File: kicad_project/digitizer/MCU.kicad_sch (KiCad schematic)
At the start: 4 parts

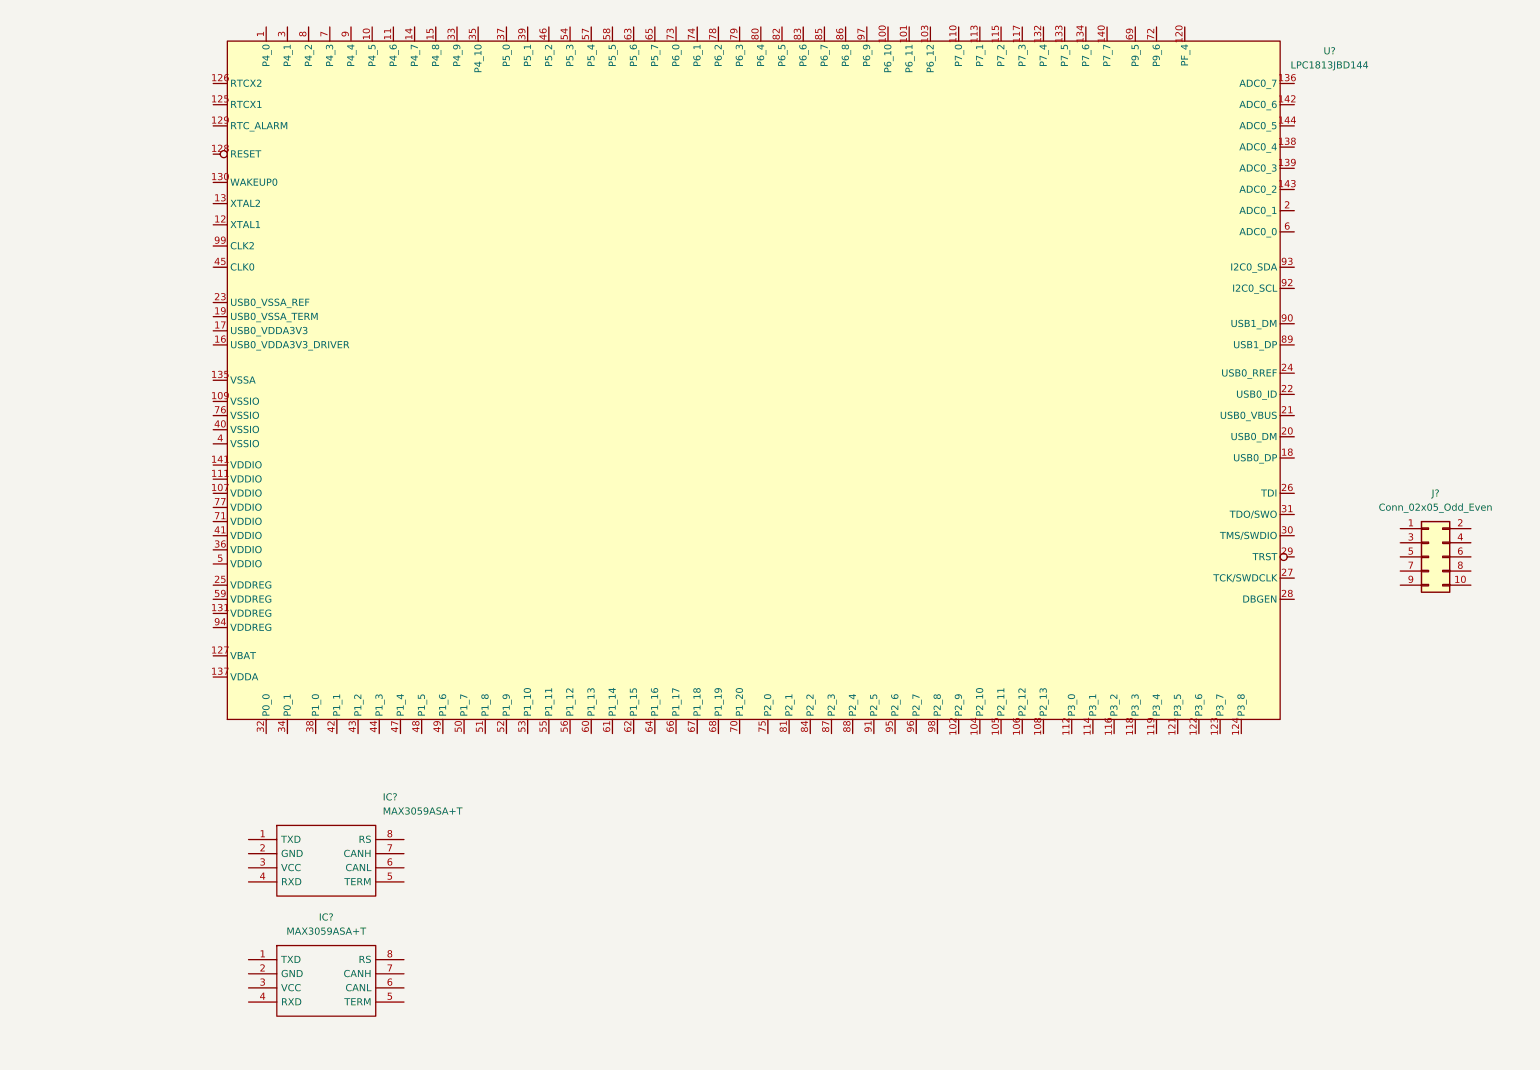
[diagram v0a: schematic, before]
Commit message: finished the CANPWR sheet, got to work on the MCU sheet (finished the CAN stuff). Good progress; still missing the MCU pin connections and the connector footprints (M12, deutsch, etc.)
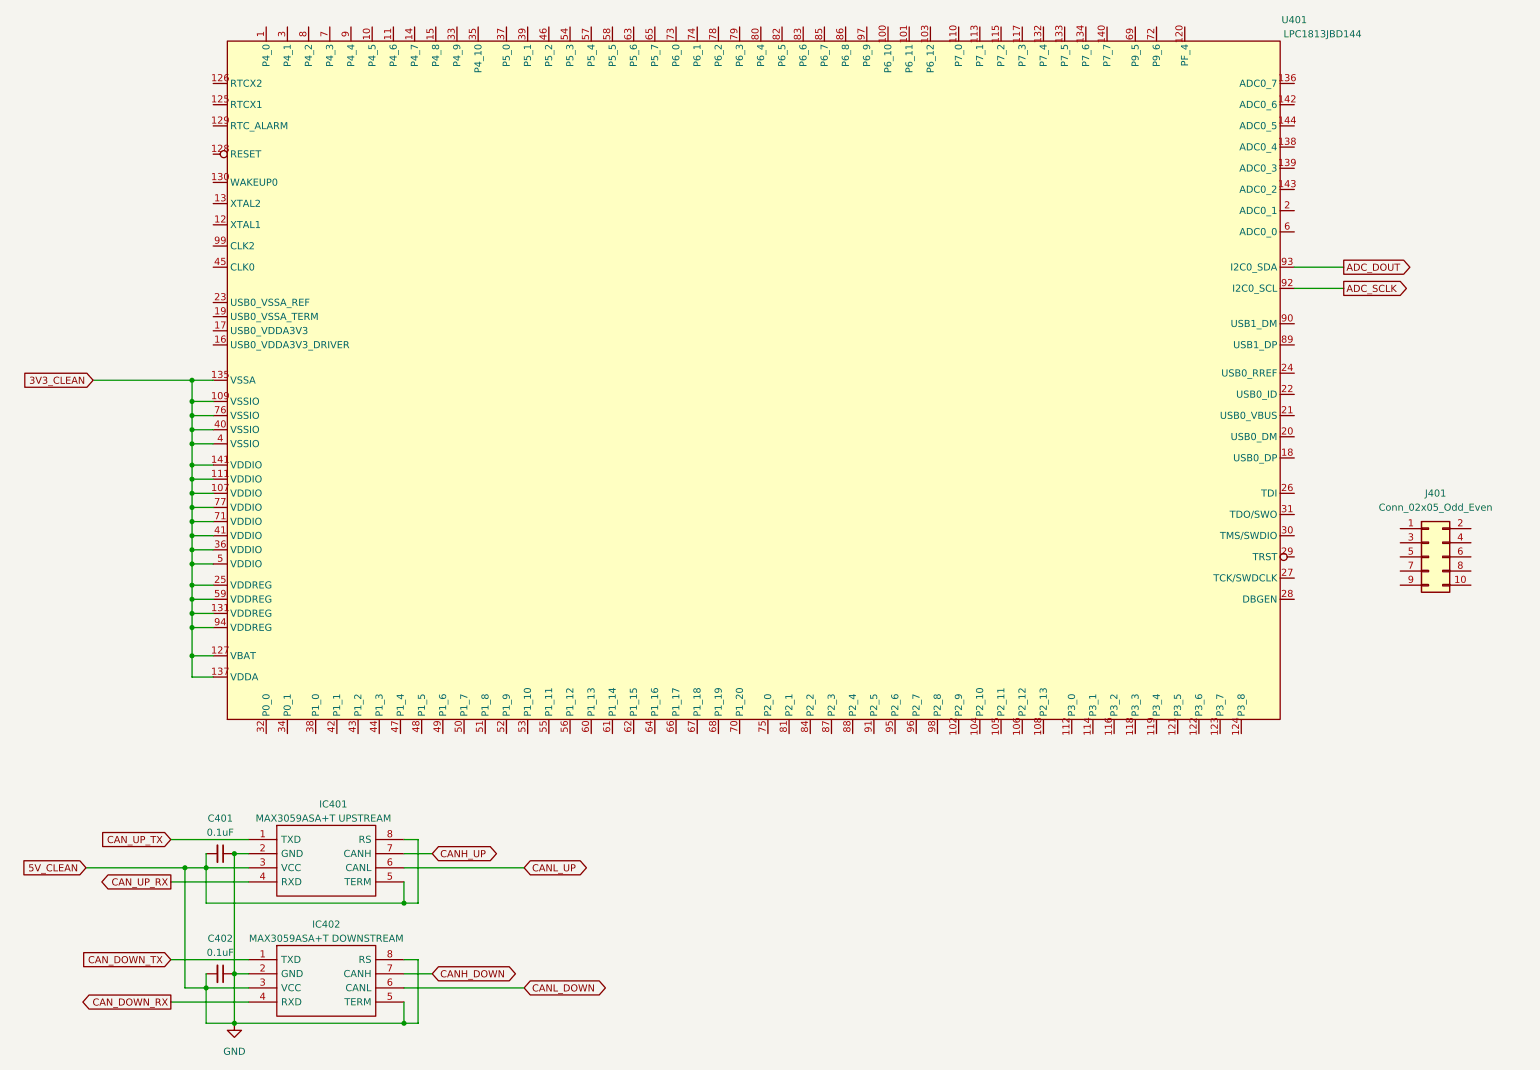
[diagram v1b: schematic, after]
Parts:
- added C401, C402: 0.1uF, Capacitor_SMD:C_2220_5650Metric_Pad1.97x5.40mm_HandSolder, symbol Device:C_Small
- IC401: renamed from IC?; value MAX3059ASA+T -> MAX3059ASA+T UPSTREAM
- IC402: renamed from IC?; value MAX3059ASA+T -> MAX3059ASA+T DOWNSTREAM
- gave numbers to parts that had none: 2
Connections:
- net CAN_DOWN_TX: now reaches IC402.1 (TXD)
- net GND: now reaches IC402.2 (GND)
- net GND: now also IC401.2 (GND), IC401.3 (VCC), IC401.5 (TERM), IC401.8 (RS), IC402.3 (VCC), IC402.5 (TERM), IC402.8 (RS), C401.1, C401.2, C402.1, C402.2
- net CAN_DOWN_RX: now reaches IC402.4 (RXD)
- net CANL_DOWN: now reaches IC402.6 (CANL)
- net CANH_DOWN: now reaches IC402.7 (CANH)
- net 3V3_CLEAN: now reaches U401.107 (VDDIO)
- net 3V3_CLEAN: now also U401.109 (VSSIO), U401.111 (VDDIO), U401.127 (VBAT), U401.131 (VDDREG), U401.135 (VSSA), U401.137 (VDDA), U401.141 (VDDIO), U401.25 (VDDREG), U401.36 (VDDIO), U401.4 (VSSIO), U401.40 (VSSIO), U401.41 (VDDIO), U401.5 (VDDIO), U401.59 (VDDREG), U401.71 (VDDIO), U401.76 (VSSIO), U401.77 (VDDIO), U401.94 (VDDREG)
- net ADC_SCLK: now reaches U401.92 (I2C0_SCL)
- net ADC_DOUT: now reaches U401.93 (I2C0_SDA)
- net CAN_UP_TX: now reaches IC401.1 (TXD)
- net CAN_UP_RX: now reaches IC401.4 (RXD)
- net CANL_UP: now reaches IC401.6 (CANL)
- net CANH_UP: now reaches IC401.7 (CANH)

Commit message: commit
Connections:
- net 3V3_CLEAN: no longer U401.109 (VSSIO), U401.135 (VSSA), U401.4 (VSSIO), U401.40 (VSSIO), U401.76 (VSSIO)
- net GND: now also U401.109 (VSSIO), U401.135 (VSSA), U401.4 (VSSIO), U401.40 (VSSIO), U401.76 (VSSIO)

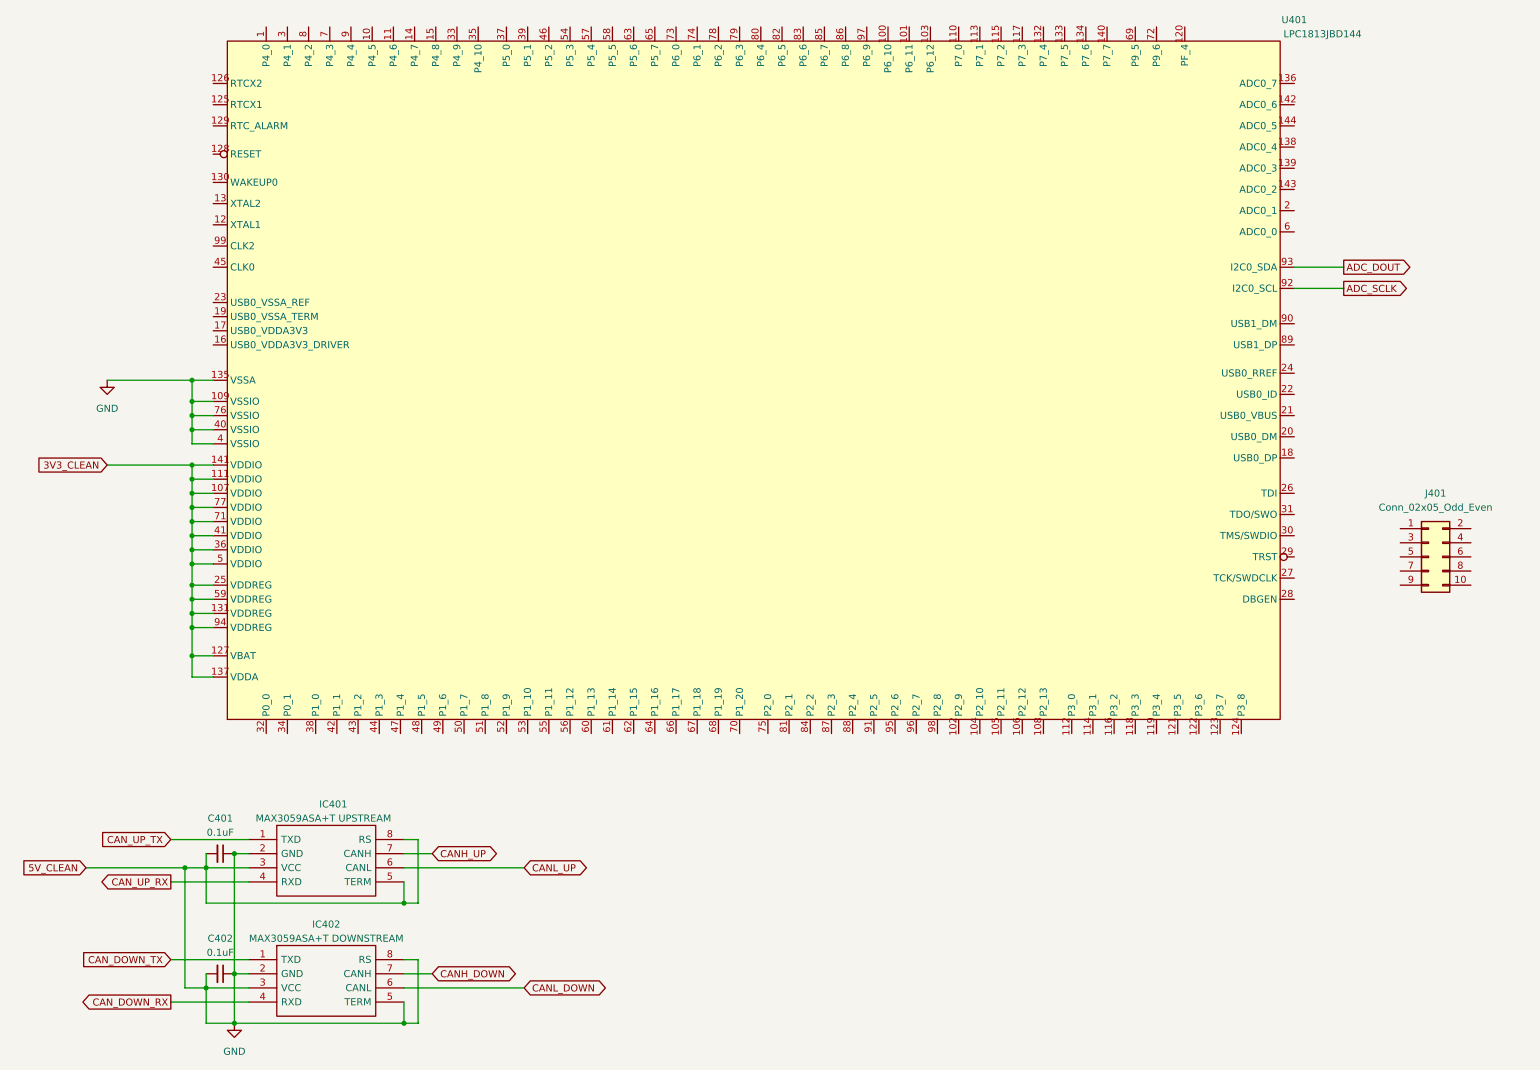
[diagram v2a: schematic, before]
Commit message: imported the correct symbols & footprints, and added a few to the schematic: pulled in the correct MCU symbol/footprint, as well as the correct JTAG footprint (connected to the 2x5 odd_even connector)
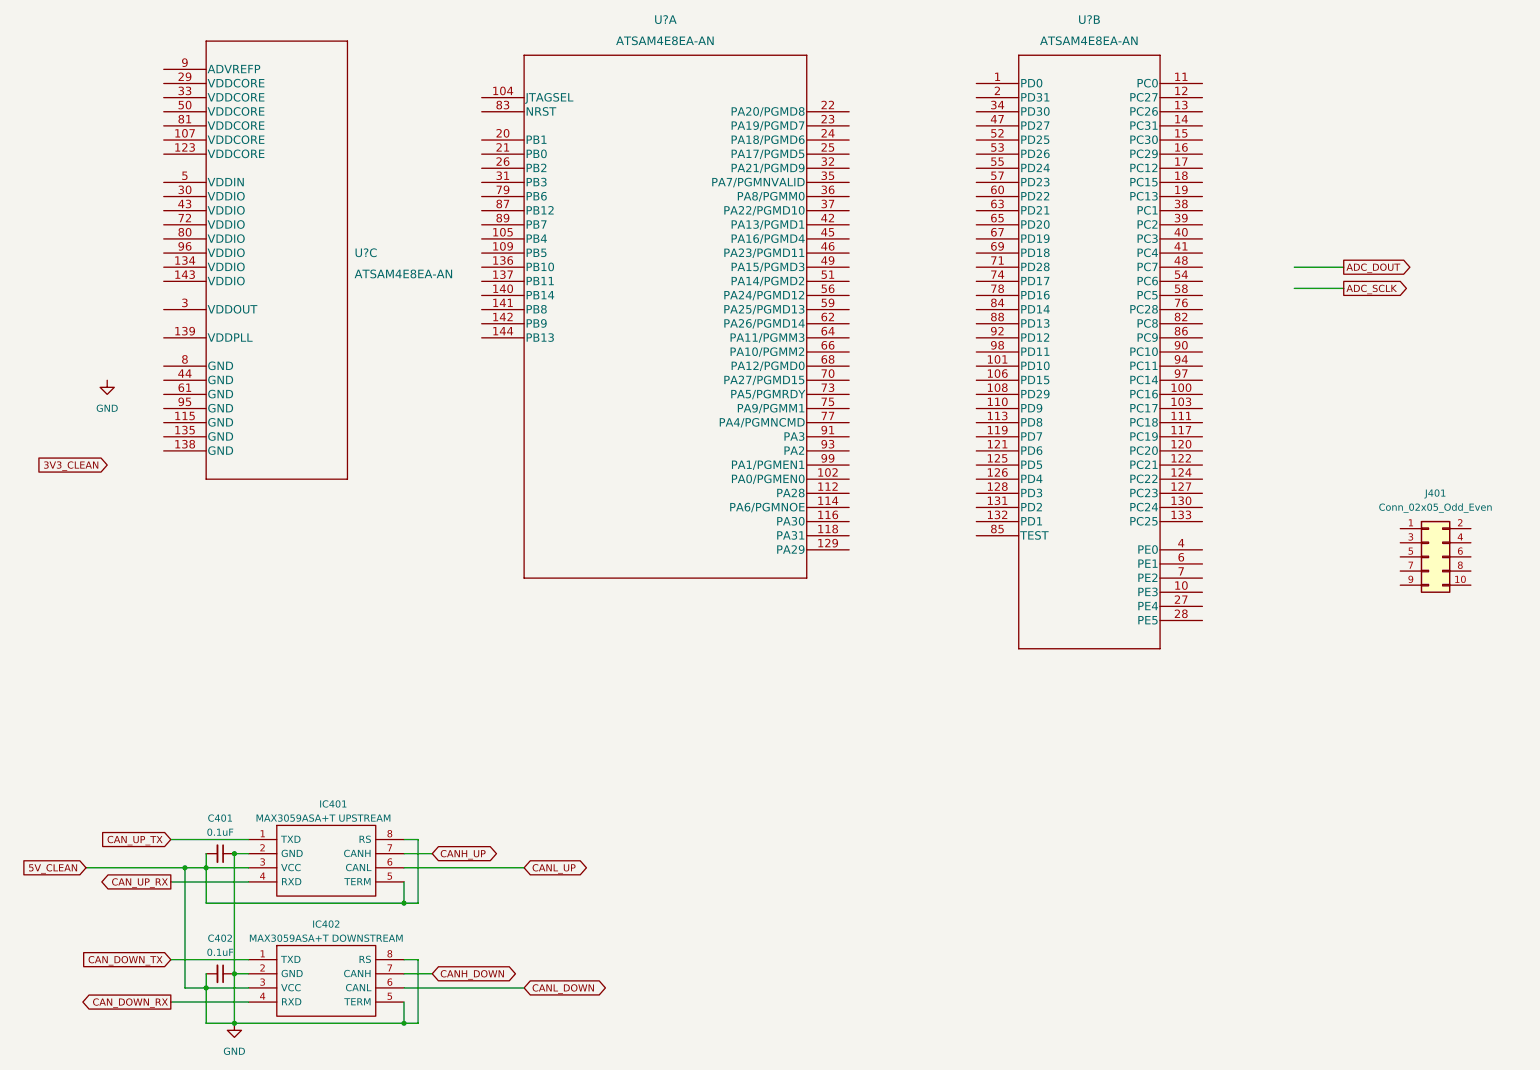
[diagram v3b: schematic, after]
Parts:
- removed U401: LPC1813JBD144, 495-project-library:LQFP-144_20x20mm_P0.5mm, symbol 495-project-library:LPC1813JBD144
- added U? (x2): ATSAM4E8EA-AN, LQFP144_20x20MC_MCH, symbol 2022-01-19_19-47-49:ATSAM4E8EA-AN
- added U?: ATSAM4E8EA-AN, footprints:ATSAM4E8EA-AN, symbol 2022-01-19_19-47-49:ATSAM4E8EA-AN
- J401: footprint (none) -> SamacSys_Parts:SHF10501LDTHTR

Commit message: moved CAN modules to the CANPWR sheet. Finished (first draft) of the MCU power design
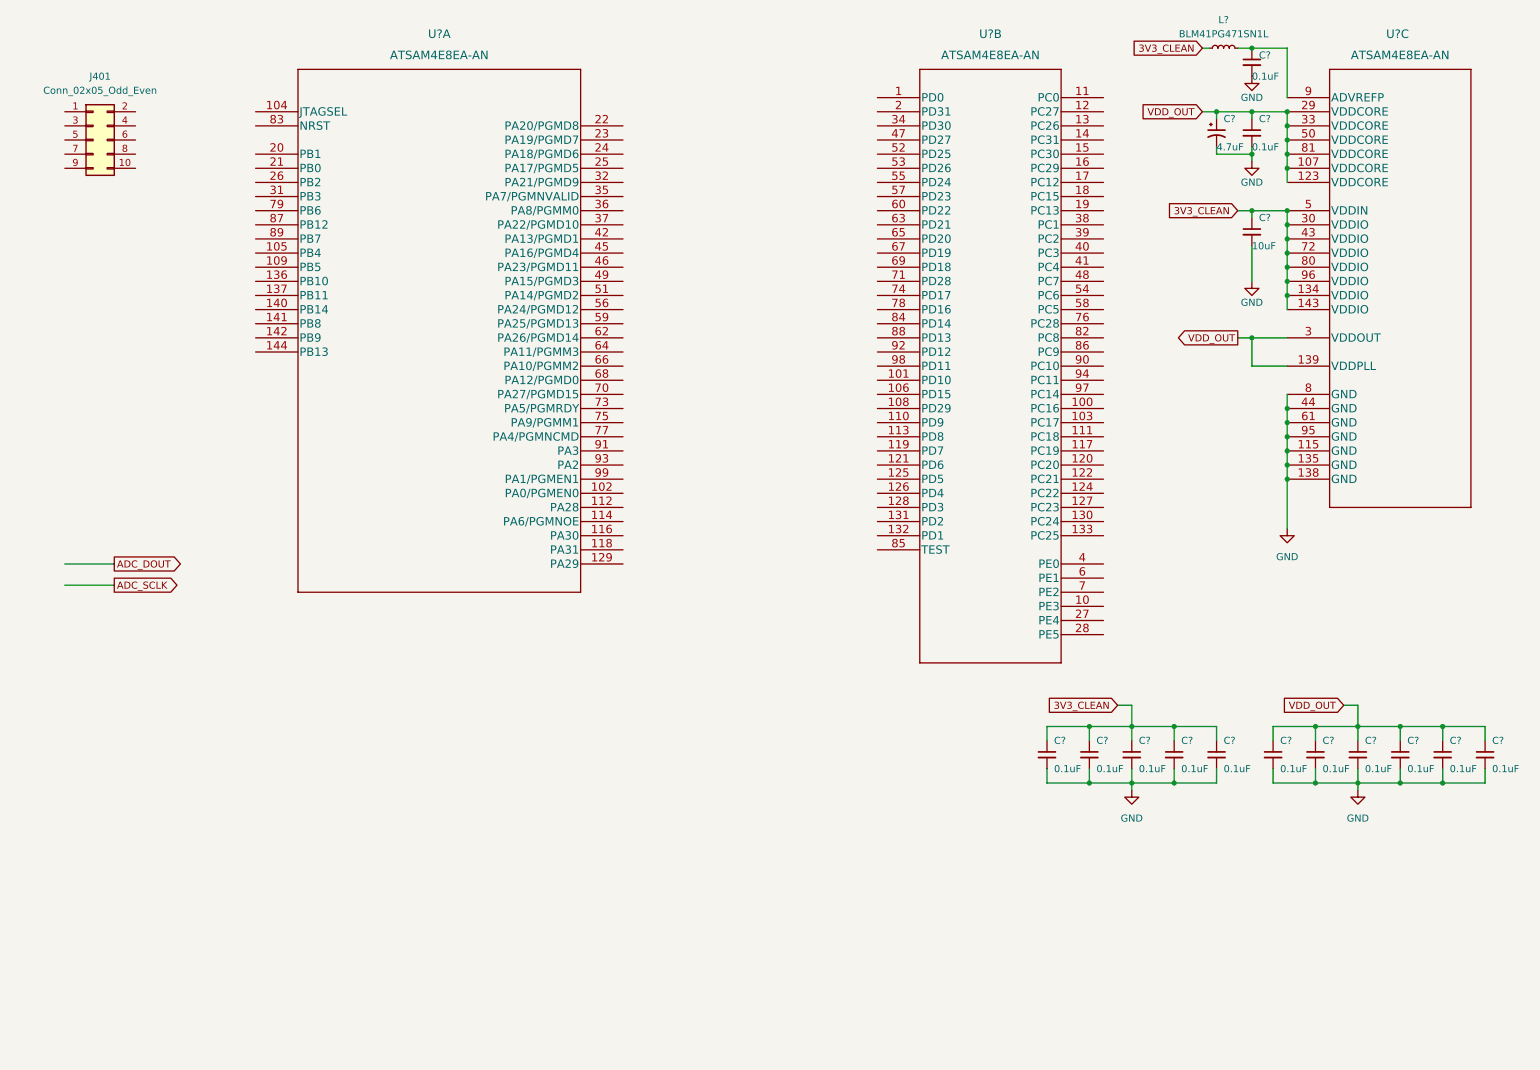
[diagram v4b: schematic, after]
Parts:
- removed C401, C402: 0.1uF, Capacitor_SMD:C_2220_5650Metric_Pad1.97x5.40mm_HandSolder, symbol Device:C_Small
- removed IC401: MAX3059ASA+T UPSTREAM, SOIC127P600X175-8N, symbol SamacSys_Parts:MAX3059ASA+T
- removed IC402: MAX3059ASA+T DOWNSTREAM, SOIC127P600X175-8N, symbol SamacSys_Parts:MAX3059ASA+T
- added C?: 10uF, Capacitor_SMD:C_2220_5650Metric_Pad1.97x5.40mm_HandSolder, symbol Device:C_Small
- added C? (x13): 0.1uF, Capacitor_SMD:C_2220_5650Metric_Pad1.97x5.40mm_HandSolder, symbol Device:C_Small
- added C?: 4.7uF, Capacitor_Tantalum_SMD:CP_EIA-6032-20_AVX-F_Pad2.25x2.35mm_HandSolder, symbol Device:C_Polarized_Small_US
- added L?: BLM41PG471SN1L, Inductor_SMD:L_1806_4516Metric_Pad1.45x1.90mm_HandSolder, symbol Device:L_Small
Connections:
- net 3V3_CLEAN: now also U?.134 (VDDIO), U?.143 (VDDIO), U?.30 (VDDIO), U?.43 (VDDIO), U?.5 (VDDIN), U?.72 (VDDIO), U?.80 (VDDIO), U?.96 (VDDIO), C?.1, C?.1, C?.1, C?.1, C?.1, C?.1, L?.1
- net GND: now also U?.115 (GND), U?.135 (GND), U?.138 (GND), U?.44 (GND), U?.61 (GND), U?.8 (GND), U?.95 (GND), C?.2, C?.2, C?.2, C?.2, C?.2, C?.2, C?.2, C?.2, C?.2, C?.2, C?.2, C?.2, C?.2, C?.2, C?.2
- net VDD_OUT: now reaches U?.107 (VDDCORE)
- net VDD_OUT: now also U?.123 (VDDCORE), U?.139 (VDDPLL), U?.29 (VDDCORE), U?.3 (VDDOUT), U?.33 (VDDCORE), U?.50 (VDDCORE), U?.81 (VDDCORE), C?.1, C?.1, C?.1, C?.1, C?.1, C?.1, C?.1, C?.1
- net at U?.9 (ADVREFP): now also C?.1, L?.2
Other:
- moved on the sheet: J401, U?A, U?B, U?C
